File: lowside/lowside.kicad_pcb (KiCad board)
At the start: 4 copper layers, 101 x 22 mm, 291 parts, among them J1 Conn_02x39_Odd_Even, U1 VNLD5090, U2 VNLD5090, U3 VNLD5090, U4 VNLD5090, U5 VNLD5090, U6 VNLD5090

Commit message: add 7th pair
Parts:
- added C13: 6.8n, Capacitor_SMD:C_0603_1608Metric, F.Cu at (111.5, 35.0)
- added C14: 6.8n, Capacitor_SMD:C_0603_1608Metric, F.Cu at (104.0, 35.0)
- added D27: D_Schottky, Diode_SMD:D_SMF, F.Cu at (112.0, 27.5)
- added D28: D_Schottky, Diode_SMD:D_SMF, F.Cu at (102.0, 27.5)
- added D29: LED, LED_SMD:LED_0603_1608Metric, F.Cu at (111.5, 32.5)
- added D30: LED, LED_SMD:LED_0603_1608Metric, F.Cu at (102.5, 32.5)
- added R39: 1k, Resistor_SMD:R_0603_1608Metric, F.Cu at (111.0, 24.0)
- added R40: 1k, Resistor_SMD:R_0603_1608Metric, F.Cu at (105.0, 24.0)
- added R41: 10k, Resistor_SMD:R_0603_1608Metric, F.Cu at (108.0, 24.0)
- added R42: 10k, Resistor_SMD:R_0603_1608Metric, F.Cu at (102.0, 24.0)
- added R43: 1k, Resistor_SMD:R_0603_1608Metric, F.Cu at (111.5, 31.0)
- added R44: 1k, Resistor_SMD:R_0603_1608Metric, F.Cu at (102.5, 31.0)
- added REF**: via-0.6, via:via-0.6, F.Cu at (21.7, 34.8)
- added REF**: via-0.6, via:via-0.6, F.Cu at (103.6, 26.2)
- added REF**: via-0.6, via:via-0.6, F.Cu at (105.6, 26.8)
- added REF**: via-0.6, via:via-0.6, F.Cu at (112.1, 26.3)
- added REF**: via-0.6, via:via-0.6, F.Cu at (113.2, 26.3)
- added REF**: via-0.6, via:via-0.6, F.Cu at (109.3, 26.8)
- added REF**: via-0.6, via:via-0.6, F.Cu at (106.9, 26.8)
- added REF**: via-0.6, via:via-0.6, F.Cu at (107.5, 27.3)
- added REF**: via-0.6, via:via-0.6, F.Cu at (108.6, 27.2)
- added REF**: via-0.6, via:via-0.6, F.Cu at (109.9, 27.4)
- added REF**: via-0.6, via:via-0.6, F.Cu at (109.1, 28.0)
- added REF**: via-0.6, via:via-0.6, F.Cu at (120.5, 33.8)
- added REF**: via-0.6, via:via-0.6, F.Cu at (108.1, 28.0)
- added REF**: via-0.6, via:via-0.6, F.Cu at (106.4, 27.4)
- added REF**: via-0.6, via:via-0.6, F.Cu at (107.1, 28.1)
- added REF**: via-0.6, via:via-0.6, F.Cu at (107.8, 28.8)
- added REF**: via-0.6, via:via-0.6, F.Cu at (108.8, 28.8)
- added REF**: via-0.6, via:via-0.6, F.Cu at (108.4, 34.2)
- added REF**: via-0.6, via:via-0.6, F.Cu at (108.4, 33.4)
- added REF**: via-0.6, via:via-0.6, F.Cu at (108.4, 32.6)
- added REF**: via-0.6, via:via-0.6, F.Cu at (108.4, 31.8)
- added REF**: via-0.6, via:via-0.6, F.Cu at (115.5, 29.7)
- added REF**: via-0.6, via:via-0.6, F.Cu at (118.5, 23.6)
- added REF**: via-0.6, via:via-0.6, F.Cu at (115.5, 25.7)
- added REF**: via-0.6, via:via-0.6, F.Cu at (115.5, 34.3)
- added REF**: via-0.6, via:via-0.6, F.Cu at (113.0, 32.5)
- added REF**: via-0.6, via:via-0.6, F.Cu at (101.3, 30.6)
- added REF**: via-0.6, via:via-0.6, F.Cu at (102.1, 32.5)
- added REF**: via-0.6, via:via-0.6, F.Cu at (103.4, 32.7)
- added REF**: via-0.6, via:via-0.6, F.Cu at (102.9, 33.4)
- added REF**: via-0.6, via:via-0.6, F.Cu at (102.9, 34.2)
- added REF**: via-0.6, via:via-0.6, F.Cu at (104.4, 28.7)
- added REF**: via-0.6, via:via-0.6, F.Cu at (105.3, 29.1)
- added REF**: via-0.6, via:via-0.6, F.Cu at (118.5, 27.7)
- added REF**: via-0.6, via:via-0.6, F.Cu at (105.1, 30.2)
- added REF**: via-0.6, via:via-0.6, F.Cu at (105.1, 31.1)
- added REF**: via-0.6, via:via-0.6, F.Cu at (105.0, 32.1)
- added REF**: via-0.6, via:via-0.6, F.Cu at (105.9, 31.9)
- added REF**: via-0.6, via:via-0.6, F.Cu at (105.9, 32.7)
- added REF**: via-0.6, via:via-0.6, F.Cu at (118.5, 31.4)
- added REF**: via-0.6, via:via-0.6, F.Cu at (119.7, 34.5)
- added REF**: via-0.6, via:via-0.6, F.Cu at (118.1, 33.9)
- added REF**: via-0.6, via:via-0.6, F.Cu at (113.0, 35.1)
- added REF**: via-0.6, via:via-0.6, F.Cu at (110.5, 26.5)
- added U7: VNLD5090, Package_SO:SO-8_3.9x4.9mm_P1.27mm, F.Cu at (107.0, 29.0)
- moved D25 4.28 mm to (118.9, 30.6)
- moved D26 4.28 mm to (116.4, 30.6)
- moved R37 4.28 mm to (118.9, 27.1)
- moved R38 4.28 mm to (116.4, 27.1)
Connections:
- J1 pad 11: Net-(J1-Pad11) -> IN1
- J1 pad 13: Net-(J1-Pad13) -> IN2
- J1 pad 19: Net-(J1-Pad19) -> IN3
- J1 pad 21: Net-(J1-Pad21) -> IN4
- J1 pad 23: Net-(J1-Pad23) -> IN5
- J1 pad 29: Net-(J1-Pad29) -> IN6
- J1 pad 33: Net-(J1-Pad33) -> IN7
- J1 pad 39: Net-(J1-Pad39) -> IN8
- J1 pad 45: Net-(J1-Pad45) -> IN9
- J1 pad 51: Net-(J1-Pad51) -> IN10
- J1 pad 55: Net-(J1-Pad55) -> IN11
- J1 pad 61: Net-(J1-Pad61) -> IN12
- J1 pad 65: Net-(J1-Pad65) -> IN13
- J1 pad 66: Net-(J1-Pad66) -> IN13
- J1 pad 67: Net-(J1-Pad67) -> OUT13
- J1 pad 68: Net-(J1-Pad68) -> OUT13
- J1 pad 69: Net-(J1-Pad69) -> OUT14
- J1 pad 70: Net-(J1-Pad70) -> OUT14
- J1 pad 71: Net-(J1-Pad71) -> IN14
- J1 pad 72: Net-(J1-Pad72) -> IN14
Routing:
- net OUT13: track 0.00 -> 19.5 mm
- net IN13: track 0.00 -> 19.4 mm, vias 0 -> 1
- net IN14: track 0.00 -> 18.7 mm, vias 0 -> 1
- net +12V: track 186.4 -> 204.6 mm, vias 7 -> 8
- net OUT14: track 0.00 -> 18.2 mm
- net +5V: track 126.3 -> 133.3 mm
- net Net-(R40-Pad1): track 0.00 -> 5.37 mm
- net Net-(R39-Pad1): track 0.00 -> 3.90 mm
- net IN9: track 17.1 -> 19.7 mm
- net IN8: track 16.7 -> 19.3 mm
- net IN7: track 18.2 -> 20.8 mm
- net IN6: track 16.4 -> 18.9 mm
- net IN5: track 18.8 -> 21.3 mm
- net IN4: track 16.5 -> 19.0 mm
- net IN3: track 19.0 -> 21.6 mm
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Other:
- board text added: "IN 13"
- board text added: "IN 14"
- board text added: "OUT 13"
- board text added: "OUT 14"

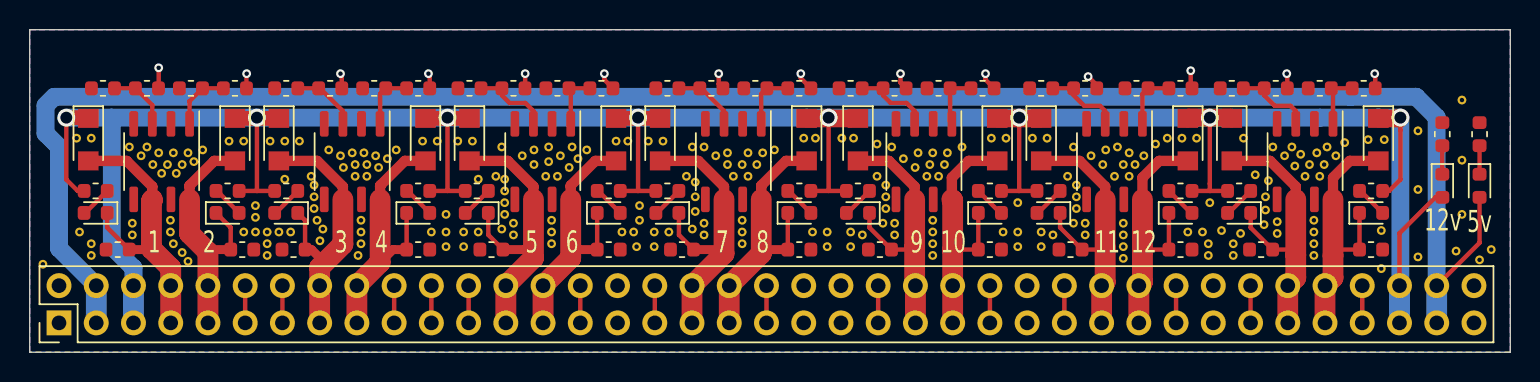
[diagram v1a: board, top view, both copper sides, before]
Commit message: Removed DRC issues.
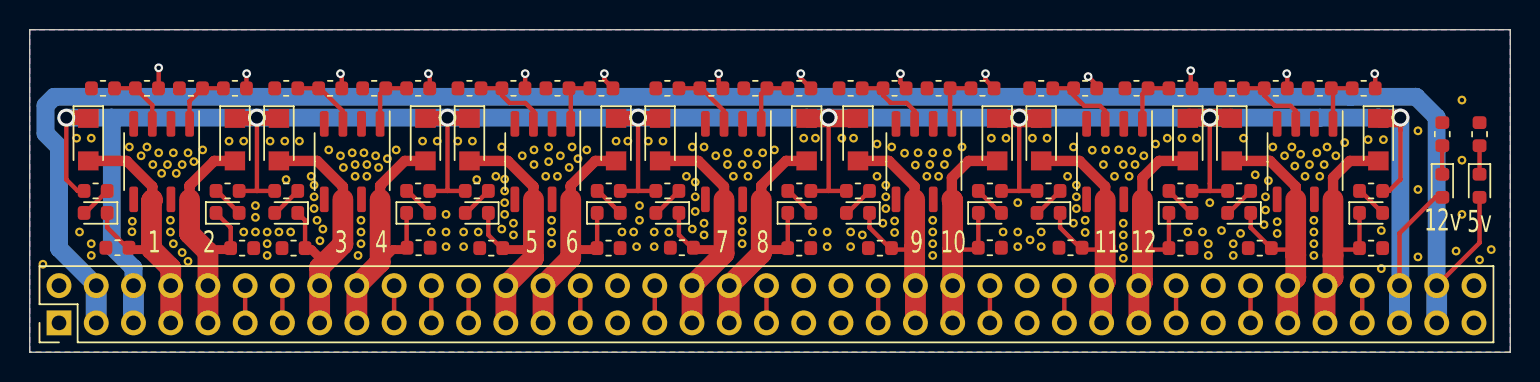
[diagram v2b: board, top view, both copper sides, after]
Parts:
- moved REF** 1.60 mm to (89.0, 33.1)
- moved REF** 0.39 mm to (93.3, 27.0)
- moved REF** 0.39 mm to (80.5, 27.2)
- moved REF** 0.23 mm to (96.0, 27.0)
- moved REF** 0.22 mm to (27.6, 32.6)
- moved REF** 0.21 mm to (95.1, 27.0)
- moved REF** 0.21 mm to (92.8, 31.8)
- moved REF** 0.17 mm to (92.8, 32.6)
- moved REF** 0.17 mm to (79.8, 32.6)
- moved REF** 0.17 mm to (81.2, 28.0)
- moved REF** 0.15 mm to (79.8, 31.8)
- moved C14 0.13 mm to (103.9, 34.9)
- moved C3 0.13 mm to (46.5, 34.9)
- moved REF** 0.13 mm to (27.6, 31.9)
- moved C2 0.13 mm to (26.0, 34.9)
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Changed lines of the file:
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@@
-(kicad_pcb (version 20171130) (host pcbnew "(5.1.5-0-10_14)")
+(kicad_pcb (version 20171130) (host pcbnew "(5.1.5)-3")
   (general
     (thickness 1.6)
@@
     (2 In2.Cu signal)
     (31 B.Cu signal)
-    (32 B.Adhes user hide)
-    (33 F.Adhes user hide)
-    (34 B.Paste user hide)
-    (35 F.Paste user hide)
+    (32 B.Adhes user)
+    (33 F.Adhes user)
+    (34 B.Paste user)
+    (35 F.Paste user)
     (36 B.SilkS user)
     (37 F.SilkS user)
-    (38 B.Mask user hide)
-    (39 F.Mask user hide)
-    (40 Dwgs.User user hide)
-    (41 Cmts.User user hide)
-    (42 Eco1.User user hide)
-    (43 Eco2.User user hide)
+    (38 B.Mask user)
+    (39 F.Mask user)
+    (40 Dwgs.User user)
+    (41 Cmts.User user)
+    (42 Eco1.User user)
+    (43 Eco2.User user)
     (44 Edge.Cuts user)
-    (45 Margin user hide)
-    (46 B.CrtYd user hide)
-    (47 F.CrtYd user hide)
-    (48 B.Fab user hide)
-    (49 F.Fab user hide)
+    (45 Margin user)
+    (46 B.CrtYd user)
+    (47 F.CrtYd user)
+    (48 B.Fab user)
+    (49 F.Fab user)
   )
   (setup
-    (last_trace_width 0.3048)
+    (last_trace_width 0.25)
     (user_trace_width 0.3048)
     (user_trace_width 0.508)
@@
     (solder_mask_min_width 0.25)
     (aux_axis_origin 0 0)
-    (visible_elements FFFFFF7F)
+    (visible_elements 7FFFFFFF)
     (pcbplotparams
       (layerselection 0x010fc_ffffffff)
@@
   )
   (module via:via-0.6 (layer F.Cu)
-    (at 113.2 26.3)
+    (at 113.1442 26.3)
     (fp_text reference REF** (at -2 0) (layer F.SilkS) hide
       (effects (font (size 0.1 0.1) (thickness 0.025)))
@@
   )
   (module Capacitor_SMD:C_0603_1608Metric (layer F.Cu)
-    (at 104 35 180)
+    (at 103.9114 34.8996 180)
     (descr "Capacitor SMD 0603 (1608 Metric), square (rectangular) end terminal, IPC_7351 nominal, (Body size source: http://www.tortai-tech.com/upload/download/2011102023233369053.pdf), generated with kicad-footprint-generator")
     (tags capacitor)
@@
   )
   (module Capacitor_SMD:C_0603_1608Metric (layer F.Cu)
-    (at 111.5 35)
+    (at 111.5 34.8996)
     (descr "Capacitor SMD 0603 (1608 Metric), square (rectangular) end terminal, IPC_7351 nominal, (Body size source: http://www.tortai-tech.com/upload/download/2011102023233369053.pdf), generated with kicad-footprint-generator")
     (tags capacitor)
@@
   )
   (module via:via-0.6 (layer F.Cu)
-    (at 95 26.8)
+    (at 95.0848 26.994)
     (fp_text reference REF** (at -2 0) (layer F.SilkS) hide
       (effects (font (size 0.1 0.1) (thickness 0.025)))
@@
   )
   (module via:via-0.6 (layer F.Cu)
-    (at 93.2 27.4)
+    (at 93.2814 27.0194)
     (fp_text reference REF** (at -2 0) (layer F.SilkS) hide
       (effects (font (size 0.1 0.1) (thickness 0.025)))
@@
   )
   (module via:via-0.6 (layer F.Cu)
-    (at 94 28)
+    (at 94.0434 28)
     (fp_text reference REF** (at -2 0) (layer F.SilkS) hide
       (effects (font (size 0.1 0.1) (thickness 0.025)))
@@
   )
   (module via:via-0.6 (layer F.Cu)
-    (at 95.8 27.2)
+    (at 95.9738 27.0448)
     (fp_text reference REF** (at -2 0) (layer F.SilkS) hide
       (effects (font (size 0.1 0.1) (thickness 0.025)))
@@
   )
   (module via:via-0.6 (layer F.Cu)
-    (at 80.4 27.6)
+    (at 80.4798 27.2226)
     (fp_text reference REF** (at -2 0) (layer F.SilkS) hide
       (effects (font (size 0.1 0.1) (thickness 0.025)))
@@
   )
   (module via:via-0.6 (layer F.Cu)
-    (at 81.2 28.2)
+    (at 81.2164 28.0354)
     (fp_text reference REF** (at -2 0) (layer F.SilkS) hide
       (effects (font (size 0.1 0.1) (thickness 0.025)))
@@
   )
   (module via:via-0.6 (layer F.Cu)
-    (at 92.8 32)
+    (at 92.7988 31.7946)
     (fp_text reference REF** (at -2 0) (layer F.SilkS) hide
       (effects (font (size 0.1 0.1) (thickness 0.025)))
@@
   )
   (module via:via-0.6 (layer F.Cu)
-    (at 92.8 32.8)
+    (at 92.7988 32.6328)
     (fp_text reference REF** (at -2 0) (layer F.SilkS) hide
       (effects (font (size 0.1 0.1) (thickness 0.025)))
@@
   )
   (module via:via-0.6 (layer F.Cu)
-    (at 90.6 32.8)
+    (at 89.0396 33.1408)
     (fp_text reference REF** (at -2 0) (layer F.SilkS) hide
       (effects (font (size 0.1 0.1) (thickness 0.025)))
@@
   )
   (module via:via-0.6 (layer F.Cu)
-    (at 79.8 32)
+    (at 79.8 31.8454)
     (fp_text reference REF** (at -2 0) (layer F.SilkS) hide
       (effects (font (size 0.1 0.1) (thickness 0.025)))
@@
   )
   (module via:via-0.6 (layer F.Cu)
-    (at 79.8 32.8)
+    (at 79.8 32.6328)
     (fp_text reference REF** (at -2 0) (layer F.SilkS) hide
       (effects (font (size 0.1 0.1) (thickness 0.025)))
@@
   )
   (module via:via-0.6 (layer F.Cu)
-    (at 51.4 29)
+    (at 51.2952 29.026)
     (fp_text reference REF** (at -2 0) (layer F.SilkS) hide
       (effects (font (size 0.1 0.1) (thickness 0.025)))
@@
   )
   (module via:via-0.6 (layer F.Cu)
-    (at 38 29)
+    (at 38.0904 29.026)
     (fp_text reference REF** (at -2 0) (layer F.SilkS) hide
       (effects (font (size 0.1 0.1) (thickness 0.025)))
@@
   )
   (module via:via-0.6 (layer F.Cu)
-    (at 27.6 32)
+    (at 27.6002 31.8708)
     (fp_text reference REF** (at -2 0) (layer F.SilkS) hide
       (effects (font (size 0.1 0.1) (thickness 0.025)))
@@
   )
   (module via:via-0.6 (layer F.Cu)
-    (at 27.6 32.8)
+    (at 27.5748 32.582)
     (fp_text reference REF** (at -2 0) (layer F.SilkS) hide
       (effects (font (size 0.1 0.1) (thickness 0.025)))
@@
   )
   (module Capacitor_SMD:C_0603_1608Metric (layer F.Cu)
-    (at 91 35 180)
+    (at 91 34.8742 180)
     (descr "Capacitor SMD 0603 (1608 Metric), square (rectangular) end terminal, IPC_7351 nominal, (Body size source: http://www.tortai-tech.com/upload/download/2011102023233369053.pdf), generated with kicad-footprint-generator")
     (tags capacitor)
@@
   )
   (module Capacitor_SMD:C_0603_1608Metric (layer F.Cu)
-    (at 98.5 35)
+    (at 98.5 34.8996)
     (descr "Capacitor SMD 0603 (1608 Metric), square (rectangular) end terminal, IPC_7351 nominal, (Body size source: http://www.tortai-tech.com/upload/download/2011102023233369053.pdf), generated with kicad-footprint-generator")
     (tags capacitor)
@@
   )
   (module Capacitor_SMD:C_0603_1608Metric (layer F.Cu)
-    (at 78 35 180)
+    (at 78 34.8996 180)
     (descr "Capacitor SMD 0603 (1608 Metric), square (rectangular) end terminal, IPC_7351 nominal, (Body size source: http://www.tortai-tech.com/upload/download/2011102023233369053.pdf), generated with kicad-footprint-generator")
     (tags capacitor)
@@
   )
   (module Capacitor_SMD:C_0603_1608Metric (layer F.Cu)
-    (at 85.5 35)
+    (at 85.4964 34.8742)
     (descr "Capacitor SMD 0603 (1608 Metric), square (rectangular) end terminal, IPC_7351 nominal, (Body size source: http://www.tortai-tech.com/upload/download/2011102023233369053.pdf), generated with kicad-footprint-generator")
     (tags capacitor)
@@
   )
   (module Capacitor_SMD:C_0603_1608Metric (layer F.Cu)
-    (at 64.5 35 180)
+    (at 64.4906 34.8742 180)
     (descr "Capacitor SMD 0603 (1608 Metric), square (rectangular) end terminal, IPC_7351 nominal, (Body size source: http://www.tortai-tech.com/upload/download/2011102023233369053.pdf), generated with kicad-footprint-generator")
     (tags capacitor)
@@
   )
   (module Capacitor_SMD:C_0603_1608Metric (layer F.Cu)
-    (at 72.5 35)
+    (at 72.4916 34.8996)
     (descr "Capacitor SMD 0603 (1608 Metric), square (rectangular) end terminal, IPC_7351 nominal, (Body size source: http://www.tortai-tech.com/upload/download/2011102023233369053.pdf), generated with kicad-footprint-generator")
     (tags capacitor)
@@
   )
   (module Capacitor_SMD:C_0603_1608Metric (layer F.Cu)
-    (at 51.5 35 180)
+    (at 51.4858 34.8996 180)
     (descr "Capacitor SMD 0603 (1608 Metric), square (rectangular) end terminal, IPC_7351 nominal, (Body size source: http://www.tortai-tech.com/upload/download/2011102023233369053.pdf), generated with kicad-footprint-generator")
     (tags capacitor)
@@
   )
   (module Capacitor_SMD:C_0603_1608Metric (layer F.Cu)
-    (at 59.5 35)
+    (at 59.4868 34.8996)
     (descr "Capacitor SMD 0603 (1608 Metric), square (rectangular) end terminal, IPC_7351 nominal, (Body size source: http://www.tortai-tech.com/upload/download/2011102023233369053.pdf), generated with kicad-footprint-generator")
     (tags capacitor)
@@
   )
   (module Capacitor_SMD:C_0603_1608Metric (layer F.Cu)
-    (at 38 35 180)
+    (at 37.9984 34.8996 180)
     (descr "Capacitor SMD 0603 (1608 Metric), square (rectangular) end terminal, IPC_7351 nominal, (Body size source: http://www.tortai-tech.com/upload/download/2011102023233369053.pdf), generated with kicad-footprint-generator")
     (tags capacitor)
@@
   )
   (module Capacitor_SMD:C_0603_1608Metric (layer F.Cu)
-    (at 46.5 35)
+    (at 46.5328 34.8742)
     (descr "Capacitor SMD 0603 (1608 Metric), square (rectangular) end terminal, IPC_7351 nominal, (Body size source: http://www.tortai-tech.com/upload/download/2011102023233369053.pdf), generated with kicad-footprint-generator")
     (tags capacitor)
@@
   )
   (module Capacitor_SMD:C_0603_1608Metric (layer F.Cu)
-    (at 26 35 180)
+    (at 25.9842 34.8742 180)
     (descr "Capacitor SMD 0603 (1608 Metric), square (rectangular) end terminal, IPC_7351 nominal, (Body size source: http://www.tortai-tech.com/upload/download/2011102023233369053.pdf), generated with kicad-footprint-generator")
     (tags capacitor)
@@
   )
   (module Capacitor_SMD:C_0603_1608Metric (layer F.Cu)
-    (at 34.5 35)
+    (at 34.4932 34.8996)
     (descr "Capacitor SMD 0603 (1608 Metric), square (rectangular) end terminal, IPC_7351 nominal, (Body size source: http://www.tortai-tech.com/upload/download/2011102023233369053.pdf), generated with kicad-footprint-generator")
     (tags capacitor)

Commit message: Generated gerbers and BOM for MFG.
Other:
- rule pad_to_mask_clearance: 0.051 -> 0.0762
- board text added: "rusEFI.com Lowside R0.1"
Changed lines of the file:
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@@
   (general
     (thickness 1.6)
-    (drawings 52)
+    (drawings 55)
     (tracks 476)
     (zones 0)
@@
     (nets 86)
   )
-  (page A4)
+  (page A)
+  (title_block
+    (date 2020-02-15)
+    (rev R0.1)
+    (company rusEFI.com)
+  )
   (layers
     (0 F.Cu signal)
@@
     (44 Edge.Cuts user)
     (45 Margin user)
-    (46 B.CrtYd user)
-    (47 F.CrtYd user)
+    (46 B.CrtYd user hide)
+    (47 F.CrtYd user hide)
     (48 B.Fab user)
     (49 F.Fab user)
@@
     (pad_size 0.6 0.6)
     (pad_drill 0.3)
-    (pad_to_mask_clearance 0.051)
-    (solder_mask_min_width 0.25)
+    (pad_to_mask_clearance 0.0762)
     (aux_axis_origin 0 0)
-    (visible_elements 7FFFFFFF)
+    (visible_elements 7FFFFF7F)
     (pcbplotparams
       (layerselection 0x010fc_ffffffff)
@@
       (outputformat 1)
       (mirror false)
-      (drillshape 1)
+      (drillshape 0)
       (scaleselection 1)
-      (outputdirectory ""))
+      (outputdirectory "gerbers/"))
   )
   (net 0 "")
@@
     )
   )
+  (dimension 22 (width 0.15) (layer Dwgs.User)
+    (gr_text "0.8661 in" (at 127.665 31 90) (layer Dwgs.User)
+      (effects (font (size 1 1) (thickness 0.15)))
+    )
+    (feature1 (pts (xy 121 20) (xy 126.951421 20)))
+    (feature2 (pts (xy 121 42) (xy 126.951421 42)))
+    (crossbar (pts (xy 126.365 42) (xy 126.365 20)))
+    (arrow1a (pts (xy 126.365 20) (xy 126.951421 21.126504)))
+    (arrow1b (pts (xy 126.365 20) (xy 125.778579 21.126504)))
+    (arrow2a (pts (xy 126.365 42) (xy 126.951421 40.873496)))
+    (arrow2b (pts (xy 126.365 42) (xy 125.778579 40.873496)))
+  )
+  (dimension 101 (width 0.15) (layer Dwgs.User)
+    (gr_text "3.9764 in" (at 70.5 46.384999) (layer Dwgs.User)
+      (effects (font (size 1 1) (thickness 0.15)))
+    )
+    (feature1 (pts (xy 121 42) (xy 121 45.67142)))
+    (feature2 (pts (xy 20 42) (xy 20 45.67142)))
+    (crossbar (pts (xy 20 45.084999) (xy 121 45.084999)))
+    (arrow1a (pts (xy 121 45.084999) (xy 119.873496 45.67142)))
+    (arrow1b (pts (xy 121 45.084999) (xy 119.873496 44.498578)))
+    (arrow2a (pts (xy 20 45.084999) (xy 21.126504 45.67142)))
+    (arrow2b (pts (xy 20 45.084999) (xy 21.126504 44.498578)))
+  )
+  (gr_text "rusEFI.com Lowside R0.1" (at 109.3724 21.5392) (layer F.SilkS)
+    (effects (font (size 1 1) (thickness 0.15)))
+  )
   (gr_text "IN 14" (at 110.8 33.8 90) (layer B.SilkS)
